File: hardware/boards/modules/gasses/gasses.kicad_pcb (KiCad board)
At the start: 2 copper layers, 95 x 75 mm, 30 parts, among them J1 Program Header, M1 MiCS-6814, U9 Buffer

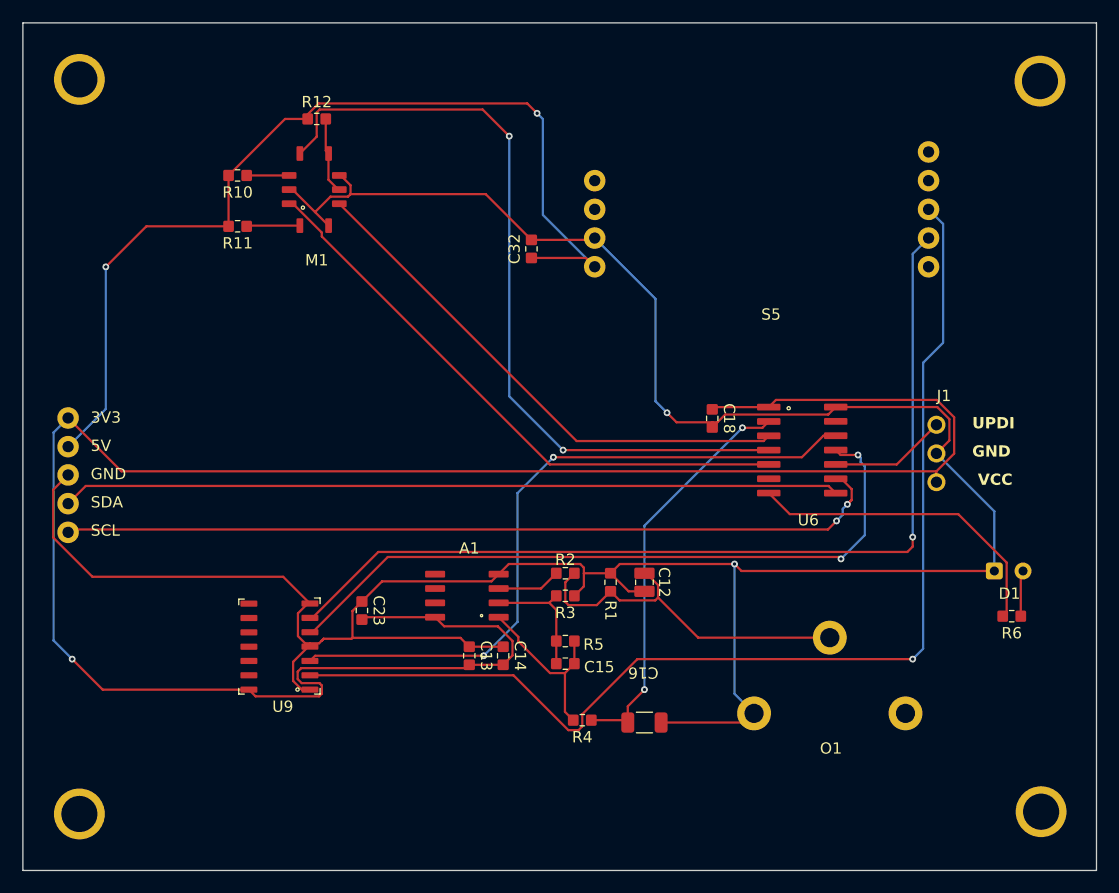
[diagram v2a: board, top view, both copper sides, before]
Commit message: redesigned gas module pcb
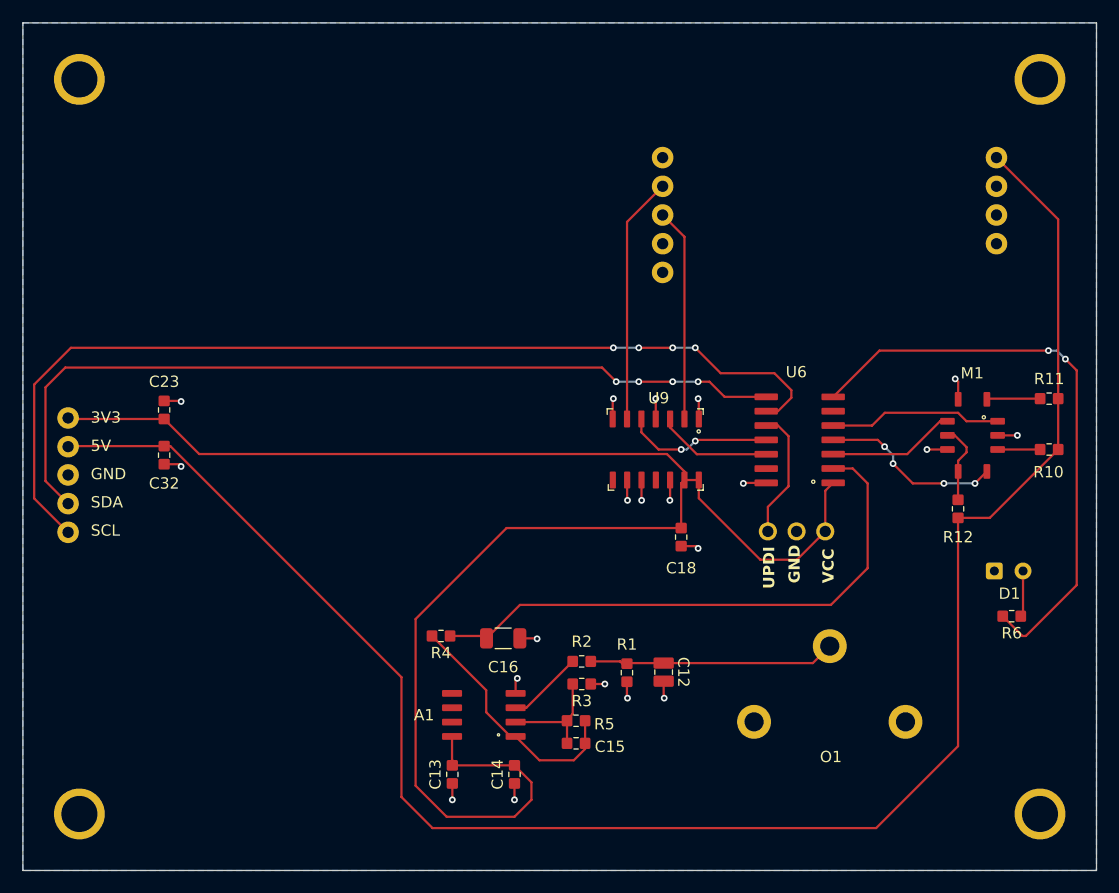
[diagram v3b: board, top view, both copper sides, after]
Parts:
- removed the REF** at (181.9, 72.8)
- removed the REF** at (182.0, 137.5)
- added ?: , , F.Cu at (182.0, 63.0)
- added ?: , , F.Cu at (182.0, 128.0)
- moved R10 75.8 mm to (182.8, 95.8), turned to 0 degrees
- moved R11 73.4 mm to (182.8, 91.2), turned to 0 degrees
- moved R12 66.4 mm to (174.8, 101.0), turned to 90 degrees
- moved M1 62.2 mm to (176.0, 94.5), turned to 180 degrees
- moved U9 37.6 mm to (148.0, 95.8), turned to 180 degrees
- moved C32 37.3 mm to (104.5, 96.2), turned to -90 degrees
- moved C23 24.9 mm to (104.5, 92.2)
- moved J1 17.0 mm to (160.5, 98.5), turned to 180 degrees
- moved C16 14.6 mm to (134.5, 112.2)
- moved R4 14.6 mm to (129.0, 112.2)
- moved U6 11.5 mm to (166.4, 93.9), turned to 90 degrees
- moved C18 10.9 mm to (150.2, 103.5)
- moved A1 10.7 mm to (138.9, 119.2)
- moved C13 10.6 mm to (130.0, 124.5), turned to 90 degrees
- moved C14 10.5 mm to (135.5, 124.5), turned to 90 degrees
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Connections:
- U9 pad 10: unconnected-(U9-3OE-Pad10) -> GND
- U9 pad 12: unconnected-(U9-4A-Pad12) -> GND
- U9 pad 13: unconnected-(U9-4OE-Pad13) -> 3V3
- U9 pad 9: unconnected-(U9-3A-Pad9) -> GND
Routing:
- net GND: track 245.3 -> 33.2 mm, vias 2 -> 20
- net CO2_TX: track 100.0 -> 18.8 mm, vias 1 -> 0
- net 5V: track 86.3 -> 161.6 mm, vias 2 -> 0
- net C02_RX: track 83.8 -> 21.9 mm, vias 1 -> 0
- net NH3_VAL: track 70.3 -> 16.1 mm, vias 2 -> 4
- net AT_GAS_RX: track 61.5 -> 10.2 mm, vias 2 -> 0
- net AT_GAS_TX: track 62.8 -> 13.2 mm
- net 3V3: track 192.6 -> 148.9 mm, vias 1 -> 0
- net NO2_VAL: track 52.2 -> 15.3 mm
- net CO_VAL: track 46.9 -> 11.3 mm
- net STATUS_LED: track 28.5 -> 52.1 mm, vias 0 -> 2
- net 02_A: track 36.2 -> 50.7 mm, vias 2 -> 0
- net SCL: track 74.7 -> 87.6 mm, vias 2 -> 4
- net Net-(O1-Vsensor+): track 31.5 -> 21.9 mm
- net SDA: track 68.8 -> 76.7 mm, vias 0 -> 4
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- added copper zone on B.Cu, net GND

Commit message: updated sensor module schematics
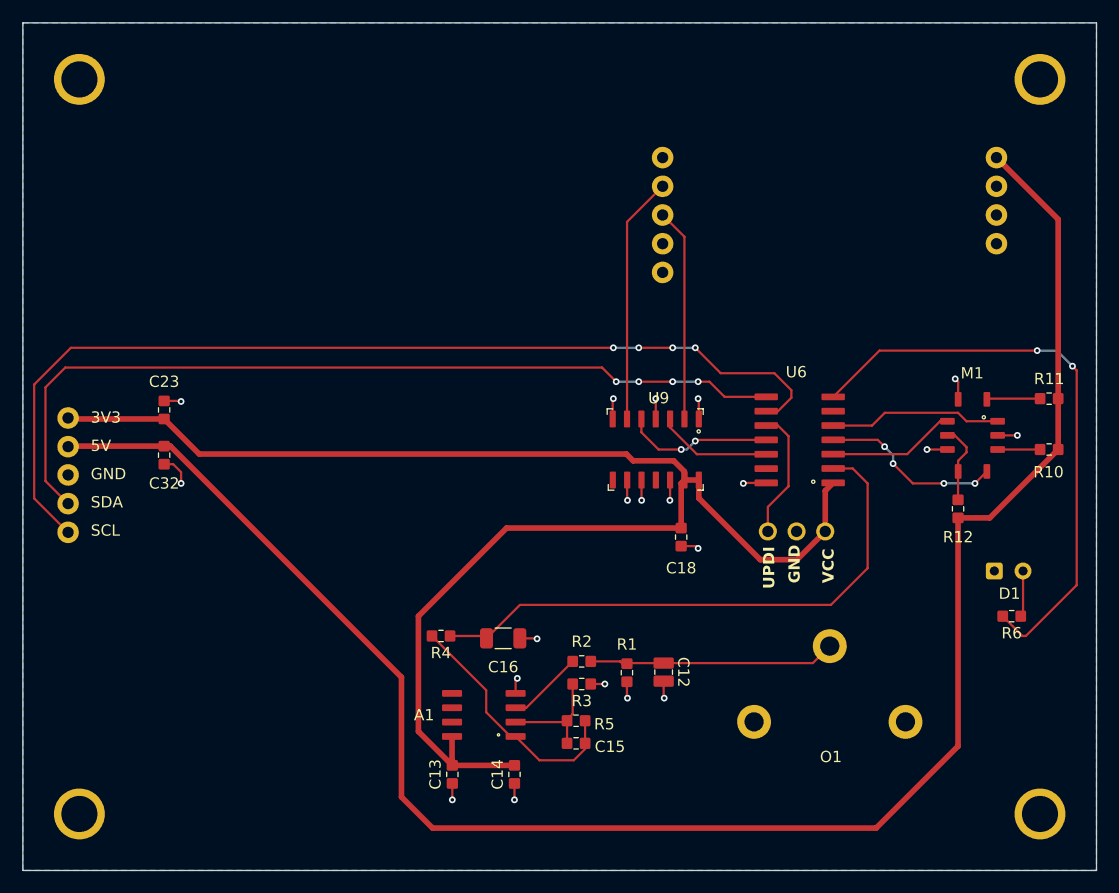
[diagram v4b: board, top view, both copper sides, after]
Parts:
- removed REF** (x2): mounting_hole, air_sens_foots:mounting_hole
- added ?: , , F.Cu at (97.0, 63.0)
- added ?: , , F.Cu at (97.0, 128.0)
- ? (x2): value (none) -> mounting_hole; footprint (none) -> air_sens_foots:mounting_hole
- moved ? 9.70 mm to (181.9, 72.7)
- moved ? 9.70 mm to (181.9, 137.7)
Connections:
- net C02_RX renamed CO2_RX
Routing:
- net 3V3: track 148.9 -> 132.6 mm
- net GND: track 33.2 -> 34.4 mm
